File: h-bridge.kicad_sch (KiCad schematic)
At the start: 20 parts, among them J2 Conn_02x06_Counter_Clockwise, M3 DC, Q3 Q_NMOS, Q4 Q_NMOS, Q5 Q_NMOS, Q6 Q_NMOS, U6 DRV8701

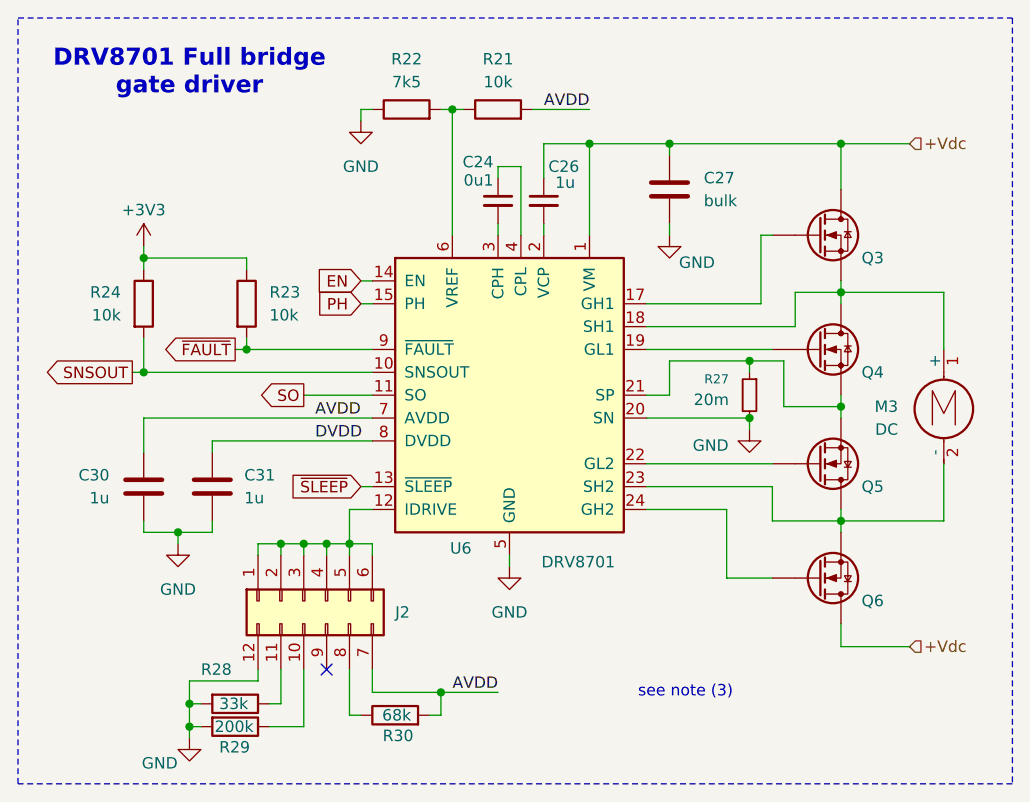
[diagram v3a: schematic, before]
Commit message: schem: renumber
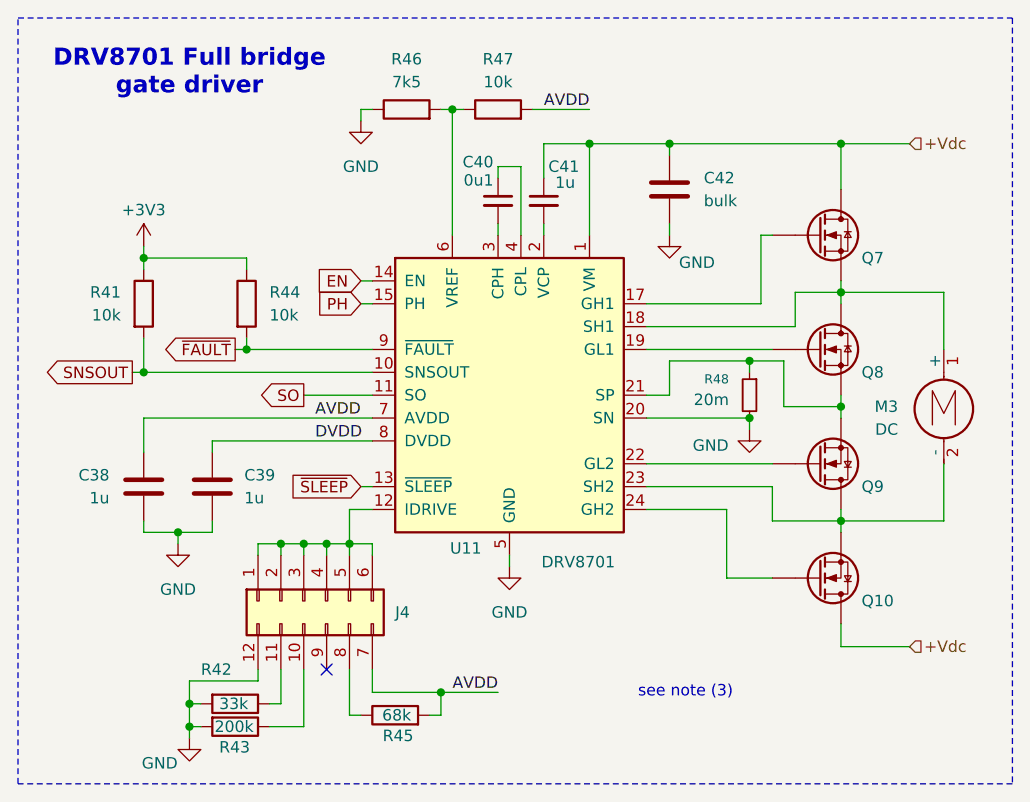
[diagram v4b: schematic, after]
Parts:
- renumbered C30 to C38, C31 to C39, C24 to C40, C26 to C41, C27 to C42, J2 to J4, Q6 to Q10, Q3 to Q7, Q4 to Q8, Q5 to Q9, R24 to R41, R28 to R42, R29 to R43, R23 to R44, R30 to R45, R22 to R46, R21 to R47, R27 to R48, U6 to U11
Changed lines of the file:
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@@
 		(dnp no)
 		(fields_autoplaced yes)
-		(property "Reference" "#PWR061"
+		(property "Reference" "#PWR082"
 			(at 130.81 62.23 0)
 			(effects
@@
 			(project ""
 				(path "/a1dc4c9e-7b20-4b66-a693-9133bc644c6b/234f18ec-899d-4a38-bb51-5ceaab0ae171"
-					(reference "#PWR061")
+					(reference "#PWR082")
 					(unit 1)
 				)
@@
 		(on_board yes)
 		(dnp no)
-		(property "Reference" "R21"
+		(property "Reference" "R47"
 			(at 146.05 49.022 90)
 			(effects
@@
 			(project ""
 				(path "/a1dc4c9e-7b20-4b66-a693-9133bc644c6b/234f18ec-899d-4a38-bb51-5ceaab0ae171"
-					(reference "R21")
+					(reference "R47")
 					(unit 1)
 				)
@@
 		(on_board yes)
 		(dnp no)
-		(property "Reference" "C30"
+		(property "Reference" "C38"
 			(at 102.87 95.2499 0)
 			(effects
@@
 			(project ""
 				(path "/a1dc4c9e-7b20-4b66-a693-9133bc644c6b/234f18ec-899d-4a38-bb51-5ceaab0ae171"
-					(reference "C30")
+					(reference "C38")
 					(unit 1)
 				)
@@
 		(on_board yes)
 		(dnp no)
-		(property "Reference" "R29"
+		(property "Reference" "R43"
 			(at 115.062 125.476 90)
 			(effects
@@
 			(project "motor-power-poc"
 				(path "/a1dc4c9e-7b20-4b66-a693-9133bc644c6b/234f18ec-899d-4a38-bb51-5ceaab0ae171"
-					(reference "R29")
+					(reference "R43")
 					(unit 1)
 				)
@@
 		(on_board yes)
 		(dnp no)
-		(property "Reference" "Q3"
+		(property "Reference" "Q7"
 			(at 186.436 71.12 0)
 			(effects
@@
 			(project "motor-power-poc"
 				(path "/a1dc4c9e-7b20-4b66-a693-9133bc644c6b/234f18ec-899d-4a38-bb51-5ceaab0ae171"
-					(reference "Q3")
+					(reference "Q7")
 					(unit 1)
 				)
@@
 		(on_board yes)
 		(dnp no)
-		(property "Reference" "C31"
+		(property "Reference" "C39"
 			(at 117.856 95.25 0)
 			(effects
@@
 			(project "motor-power-poc"
 				(path "/a1dc4c9e-7b20-4b66-a693-9133bc644c6b/234f18ec-899d-4a38-bb51-5ceaab0ae171"
-					(reference "C31")
+					(reference "C39")
 					(unit 1)
 				)
@@
 		(on_board yes)
 		(dnp no)
-		(property "Reference" "C26"
+		(property "Reference" "C41"
 			(at 151.638 60.96 0)
 			(effects
@@
 			(project "motor-power-poc"
 				(path "/a1dc4c9e-7b20-4b66-a693-9133bc644c6b/234f18ec-899d-4a38-bb51-5ceaab0ae171"
-					(reference "C26")
+					(reference "C41")
 					(unit 1)
 				)
@@
 		(on_board yes)
 		(dnp no)
-		(property "Reference" "R22"
+		(property "Reference" "R46"
 			(at 135.89 49.022 90)
 			(effects
@@
 			(project "motor-power-poc"
 				(path "/a1dc4c9e-7b20-4b66-a693-9133bc644c6b/234f18ec-899d-4a38-bb51-5ceaab0ae171"
-					(reference "R22")
+					(reference "R46")
 					(unit 1)
 				)
@@
 		(dnp no)
 		(fields_autoplaced yes)
-		(property "Reference" "C27"
+		(property "Reference" "C42"
 			(at 168.91 62.2299 0)
 			(effects
@@
 			(project "motor-power-poc"
 				(path "/a1dc4c9e-7b20-4b66-a693-9133bc644c6b/234f18ec-899d-4a38-bb51-5ceaab0ae171"
-					(reference "C27")
+					(reference "C42")
 					(unit 1)
 				)
@@
 		(dnp no)
 		(fields_autoplaced yes)
-		(property "Reference" "#PWR062"
+		(property "Reference" "#PWR080"
 			(at 110.49 109.22 0)
 			(effects
@@
 			(project "motor-power-poc"
 				(path "/a1dc4c9e-7b20-4b66-a693-9133bc644c6b/234f18ec-899d-4a38-bb51-5ceaab0ae171"
-					(reference "#PWR062")
+					(reference "#PWR080")
 					(unit 1)
 				)
@@
 		(on_board yes)
 		(dnp no)
-		(property "Reference" "R27"
+		(property "Reference" "R48"
 			(at 171.704 84.582 0)
 			(effects
@@
 			(project ""
 				(path "/a1dc4c9e-7b20-4b66-a693-9133bc644c6b/234f18ec-899d-4a38-bb51-5ceaab0ae171"
-					(reference "R27")
+					(reference "R48")
 					(unit 1)
 				)
@@
 		(on_board yes)
 		(dnp no)
-		(property "Reference" "R30"
+		(property "Reference" "R45"
 			(at 136.652 124.206 90)
 			(effects
@@
 			(project "motor-power-poc"
 				(path "/a1dc4c9e-7b20-4b66-a693-9133bc644c6b/234f18ec-899d-4a38-bb51-5ceaab0ae171"
-					(reference "R30")
+					(reference "R45")
 					(unit 1)
 				)
@@
 		(dnp no)
 		(fields_autoplaced yes)
-		(property "Reference" "J2"
+		(property "Reference" "J4"
 			(at 134.62 110.4899 90)
 			(effects
@@
 			(project ""
 				(path "/a1dc4c9e-7b20-4b66-a693-9133bc644c6b/234f18ec-899d-4a38-bb51-5ceaab0ae171"
-					(reference "J2")
+					(reference "J4")
 					(unit 1)
 				)
@@
 		(on_board yes)
 		(dnp no)
-		(property "Reference" "#PWR066"
+		(property "Reference" "#PWR081"
 			(at 111.76 130.81 0)
 			(effects
@@
 			(project "motor-power-poc"
 				(path "/a1dc4c9e-7b20-4b66-a693-9133bc644c6b/234f18ec-899d-4a38-bb51-5ceaab0ae171"
-					(reference "#PWR066")
+					(reference "#PWR081")
 					(unit 1)
 				)
@@
 		(on_board yes)
 		(dnp no)
-		(property "Reference" "R28"
+		(property "Reference" "R42"
 			(at 113.03 116.84 90)
 			(effects
@@
 			(project ""
 				(path "/a1dc4c9e-7b20-4b66-a693-9133bc644c6b/234f18ec-899d-4a38-bb51-5ceaab0ae171"
-					(reference "R28")
+					(reference "R42")
 					(unit 1)
 				)
@@
 		(dnp no)
 		(fields_autoplaced yes)
-		(property "Reference" "R23"
+		(property "Reference" "R44"
 			(at 120.65 74.9299 0)
 			(effects
@@
 			(project ""
 				(path "/a1dc4c9e-7b20-4b66-a693-9133bc644c6b/234f18ec-899d-4a38-bb51-5ceaab0ae171"
-					(reference "R23")
+					(reference "R44")
 					(unit 1)
 				)
@@
 		(on_board yes)
 		(dnp no)
-		(property "Reference" "Q5"
+		(property "Reference" "Q9"
 			(at 186.436 96.5202 0)
 			(effects
@@
 			(project "motor-power-poc"
 				(path "/a1dc4c9e-7b20-4b66-a693-9133bc644c6b/234f18ec-899d-4a38-bb51-5ceaab0ae171"
-					(reference "Q5")
+					(reference "Q9")
 					(unit 1)
 				)
@@
 		(on_board yes)
 		(dnp no)
-		(property "Reference" "C24"
+		(property "Reference" "C40"
 			(at 145.542 60.452 0)
 			(effects
@@
 			(project ""
 				(path "/a1dc4c9e-7b20-4b66-a693-9133bc644c6b/234f18ec-899d-4a38-bb51-5ceaab0ae171"
-					(reference "C24")
+					(reference "C40")
 					(unit 1)
 				)
@@
 		(on_board yes)
 		(dnp no)
-		(property "Reference" "#PWR065"
+		(property "Reference" "#PWR085"
 			(at 173.99 96.52 0)
 			(effects
@@
 			(project ""
 				(path "/a1dc4c9e-7b20-4b66-a693-9133bc644c6b/234f18ec-899d-4a38-bb51-5ceaab0ae171"
-					(reference "#PWR065")
+					(reference "#PWR085")
 					(unit 1)
 				)
@@
 		(on_board yes)
 		(dnp no)
-		(property "Reference" "Q6"
+		(property "Reference" "Q10"
 			(at 186.436 109.2202 0)
 			(effects
@@
 			(project "motor-power-poc"
 				(path "/a1dc4c9e-7b20-4b66-a693-9133bc644c6b/234f18ec-899d-4a38-bb51-5ceaab0ae171"
-					(reference "Q6")
+					(reference "Q10")
 					(unit 1)
 				)
@@
 		(on_board yes)
 		(dnp no)
-		(property "Reference" "#PWR060"
+		(property "Reference" "#PWR084"
 			(at 165.1 74.93 0)
 			(effects
@@
 			(project ""
 				(path "/a1dc4c9e-7b20-4b66-a693-9133bc644c6b/234f18ec-899d-4a38-bb51-5ceaab0ae171"
-					(reference "#PWR060")
+					(reference "#PWR084")
 					(unit 1)
 				)
@@
 		(on_board yes)
 		(dnp no)
-		(property "Reference" "Q4"
+		(property "Reference" "Q8"
 			(at 186.436 83.82 0)
 			(effects
@@
 			(project "motor-power-poc"
 				(path "/a1dc4c9e-7b20-4b66-a693-9133bc644c6b/234f18ec-899d-4a38-bb51-5ceaab0ae171"
-					(reference "Q4")
+					(reference "Q8")
 					(unit 1)
 				)
@@
 		(on_board yes)
 		(dnp no)
-		(property "Reference" "R24"
+		(property "Reference" "R41"
 			(at 104.14 74.9299 0)
 			(effects
@@
 			(project ""
 				(path "/a1dc4c9e-7b20-4b66-a693-9133bc644c6b/234f18ec-899d-4a38-bb51-5ceaab0ae171"
-					(reference "R24")
+					(reference "R41")
 					(unit 1)
 				)
@@
 		(dnp no)
 		(fields_autoplaced yes)
-		(property "Reference" "#PWR058"
+		(property "Reference" "#PWR083"
 			(at 147.32 111.76 0)
 			(effects
@@
 			(project ""
 				(path "/a1dc4c9e-7b20-4b66-a693-9133bc644c6b/234f18ec-899d-4a38-bb51-5ceaab0ae171"
-					(reference "#PWR058")
+					(reference "#PWR083")
 					(unit 1)
 				)
@@
 		(on_board yes)
 		(dnp no)
-		(property "Reference" "U6"
+		(property "Reference" "U11"
 			(at 140.716 103.378 0)
 			(effects
@@
 			(project ""
 				(path "/a1dc4c9e-7b20-4b66-a693-9133bc644c6b/234f18ec-899d-4a38-bb51-5ceaab0ae171"
-					(reference "U6")
+					(reference "U11")
 					(unit 1)
 				)
@@
 		(on_board yes)
 		(dnp no)
-		(property "Reference" "#PWR063"
+		(property "Reference" "#PWR079"
 			(at 106.68 73.66 0)
 			(effects
@@
 			(project "motor-power-poc"
 				(path "/a1dc4c9e-7b20-4b66-a693-9133bc644c6b/234f18ec-899d-4a38-bb51-5ceaab0ae171"
-					(reference "#PWR063")
-					(unit 1)
-				)
+					(reference "#PWR079")
+					(unit 1)
+				)

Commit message: schem: run and fix ERC
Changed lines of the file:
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@@
 	)
 	(junction
+		(at 140.97 64.77)
+		(diameter 0)
+		(color 0 0 0 0)
+	)
+	(junction
 		(at 184.15 58.42)
 		(diameter 0)
@@
 	(wire
 		(pts
+			(xy 140.97 64.77) (xy 140.97 68.58)
+		)
+		(stroke
+			(width 0)
+			(type default)
+		)
+	)
+	(wire
+		(pts
 			(xy 184.15 114.3) (xy 184.15 111.76)
 		)
@@
 	(wire
 		(pts
-			(xy 140.97 54.61) (xy 140.97 68.58)
-		)
-		(stroke
-			(width 0)
-			(type default)
-		)
-	)
-	(wire
-		(pts
 			(xy 130.81 73.66) (xy 132.08 73.66)
 		)
@@
 	(wire
 		(pts
+			(xy 140.97 54.61) (xy 140.97 64.77)
+		)
+		(stroke
+			(width 0)
+			(type default)
+		)
+	)
+	(wire
+		(pts
 			(xy 140.97 54.61) (xy 142.24 54.61)
 		)
@@
 					(unit 1)
 				)
+			)
+		)
+	)
+	(symbol
+		(lib_id "power:PWR_FLAG")
+		(at 140.97 64.77 90)
+		(unit 1)
+		(exclude_from_sim no)
+		(in_bom yes)
+		(on_board yes)
+		(dnp no)
+		(fields_autoplaced yes)
+		(property "Reference" "#FLG04"
+			(at 139.065 64.77 0)
+			(effects
+				(font
+					(size 1.27 1.27)
+				)
+				(hide yes)
+			)
+		)
+		(property "Value" "PWR_FLAG"
+			(at 135.89 64.77 0)
+			(effects
+				(font
+					(size 1.27 1.27)
+				)
+				(hide yes)
+			)
+		)
+		(property "Footprint" ""
+			(at 140.97 64.77 0)
+			(effects
+				(font
+					(size 1.27 1.27)
+				)
+				(hide yes)
+			)
+		)
+		(property "Datasheet" "~"
+			(at 140.97 64.77 0)
+			(effects
+				(font
+					(size 1.27 1.27)
+				)
+				(hide yes)
+			)
+		)
+		(property "Description" "Special symbol for telling ERC where power comes from"
+			(at 140.97 64.77 0)
+			(effects
+				(font
+					(size 1.27 1.27)
+				)
+				(hide yes)
+			)
+		)
+		(pin "1"
+		)
+		(instances
+			(project "motor-power-poc"
+				(path "/a1dc4c9e-7b20-4b66-a693-9133bc644c6b/234f18ec-899d-4a38-bb51-5ceaab0ae171"
+					(reference "#FLG04")
+					(unit 1)
+				)

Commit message: schem: add title
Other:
- company: (none) -> Rémi Ait-Younes
- title: (none) -> Motor Power POC
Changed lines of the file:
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@@
 	(generator_version "9.0")
 	(paper "A4")
+	(title_block
+		(title "Motor Power POC")
+		(date "2025-11-30")
+		(rev "01")
+		(company "Rémi Ait-Younes")
+	)
 	(rectangle
 		(start 92.71 44.45)
